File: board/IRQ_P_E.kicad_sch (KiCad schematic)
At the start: 18 parts, among them IC5 74LS189, IC6 74LS189, IC7 74LS189, IC8 74LS189, U42 74157, U43 74157, U44 74148, U45 74148, U46 74F32

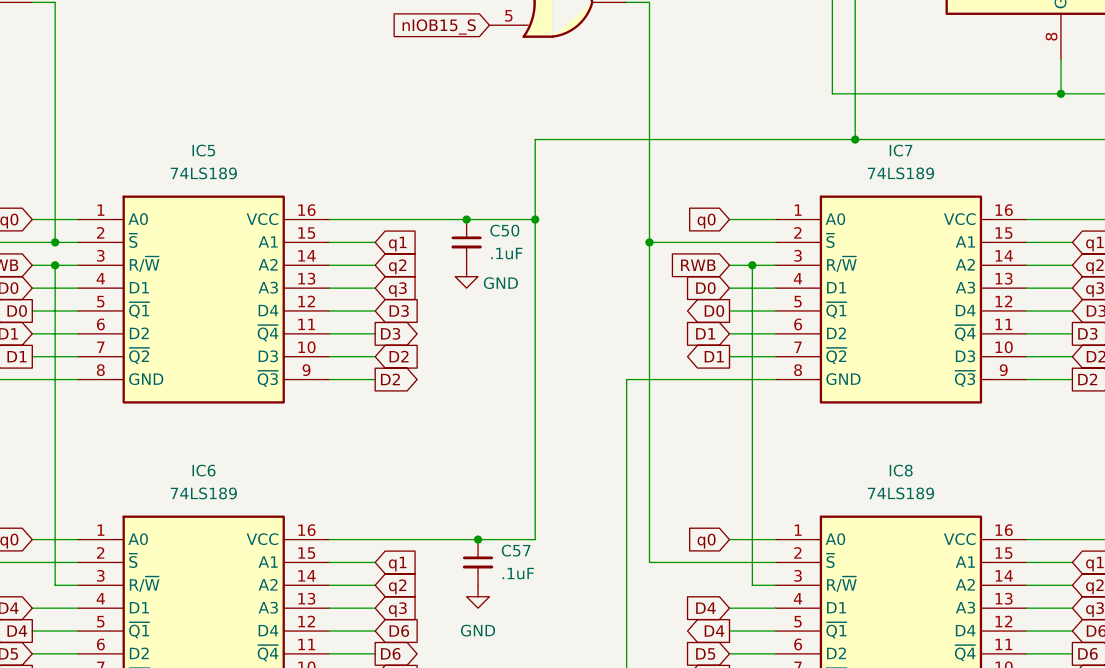
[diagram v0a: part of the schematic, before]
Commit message: Motherboard update with fill and traces.
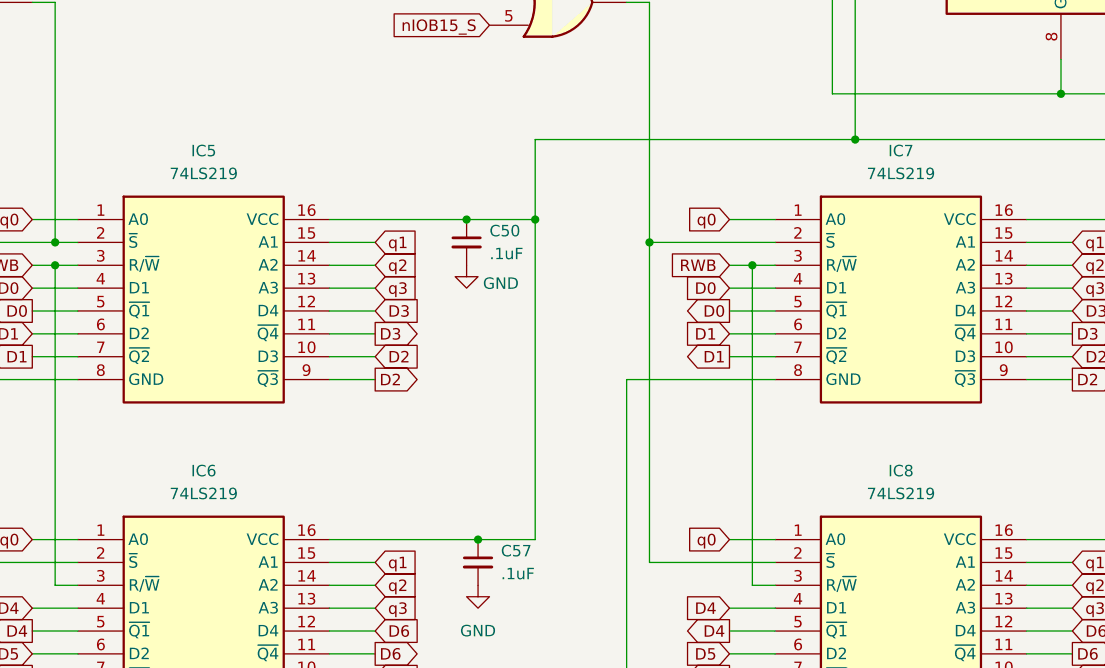
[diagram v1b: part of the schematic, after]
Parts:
- IC5, IC6, IC7, IC8: value 74LS189 -> 74LS219
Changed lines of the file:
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@@
 			)
 		)
-		(property "Value" "74LS189"
+		(property "Value" "74LS219"
 			(at 60.96 124.46 0)
 			(effects
@@
 			)
 		)
-		(property "Value" "74LS189"
+		(property "Value" "74LS219"
 			(at 60.96 160.02 0)
 			(effects
@@
 			)
 		)
-		(property "Value" "74LS189"
+		(property "Value" "74LS219"
 			(at 138.43 124.46 0)
 			(effects
@@
 			)
 		)
-		(property "Value" "74LS189"
+		(property "Value" "74LS219"
 			(at 138.43 160.02 0)
 			(effects

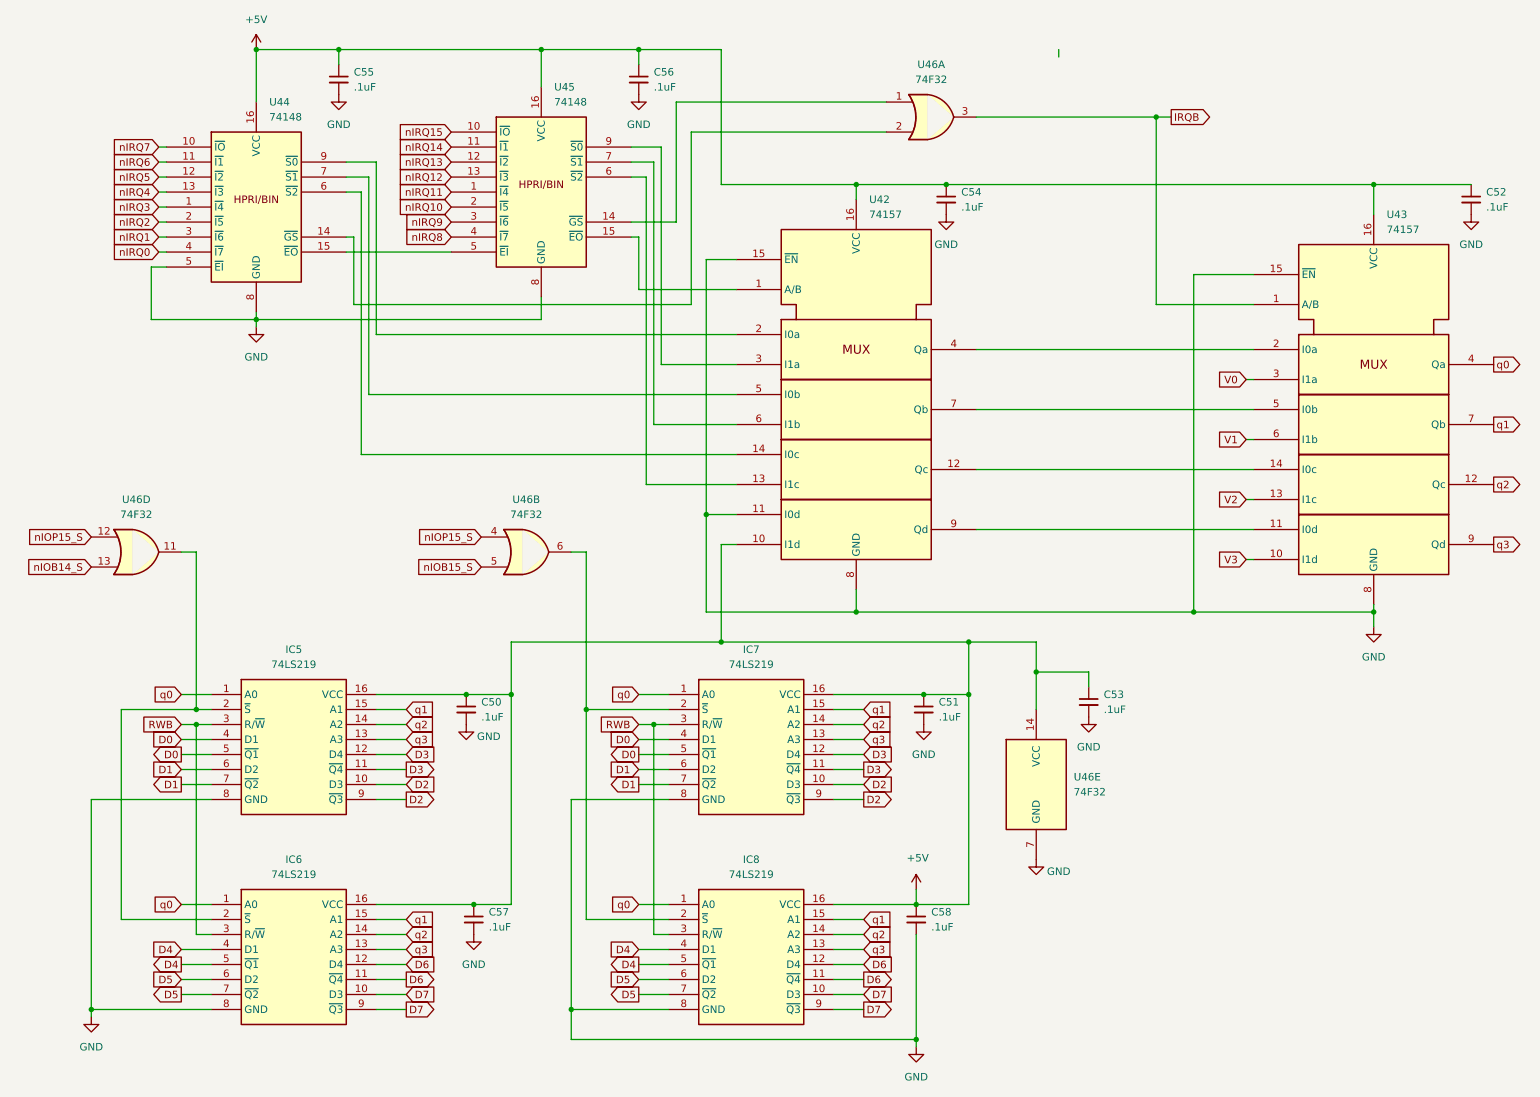
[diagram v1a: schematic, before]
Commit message: More main PCB updates.  Rearranged some things.  Bypass caps near PS connector.  Moved front panel connector to opposite side of board.
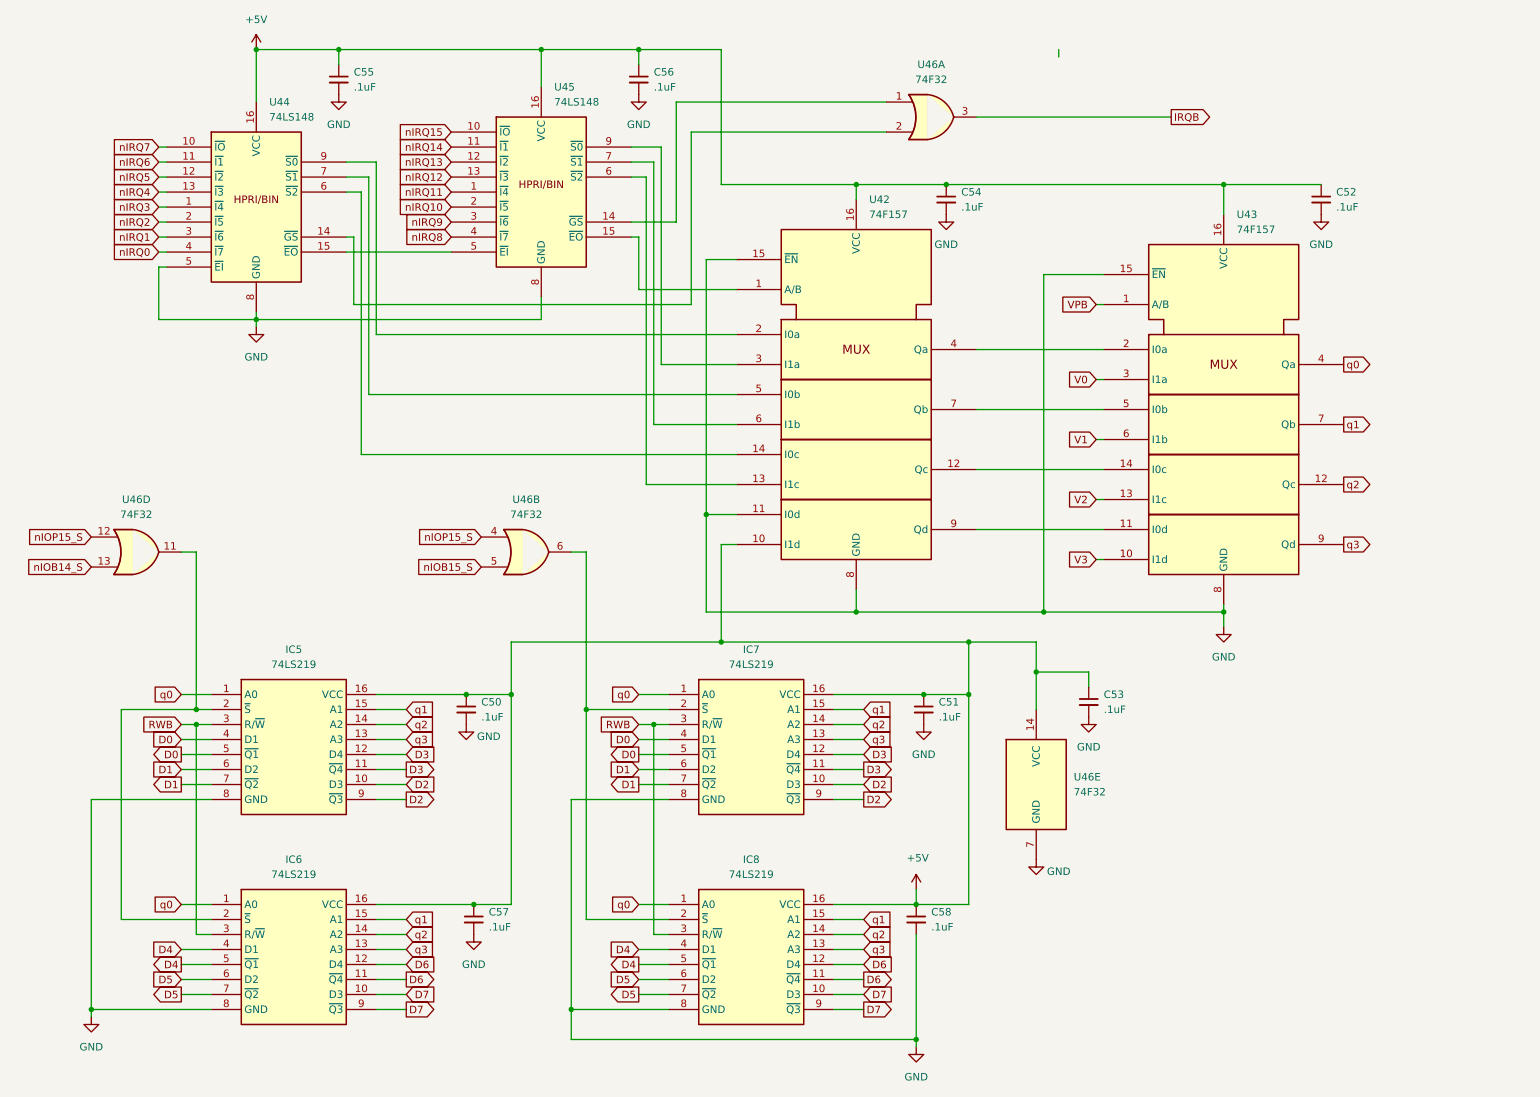
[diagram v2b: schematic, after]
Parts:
- IC5, IC6, IC7, IC8: footprint Package_DIP:DIP-16_W7.62mm_LongPads -> Package_DIP:DIP-16_W7.62mm_Socket_LongPads
- U42, U43: value 74157 -> 74F157
- U44, U45: value 74148 -> 74LS148
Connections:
- net IRQB: no longer U43.1 (A/B)
- new net VPB: U43.1 (A/B)
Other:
- moved on the sheet: C52, U43

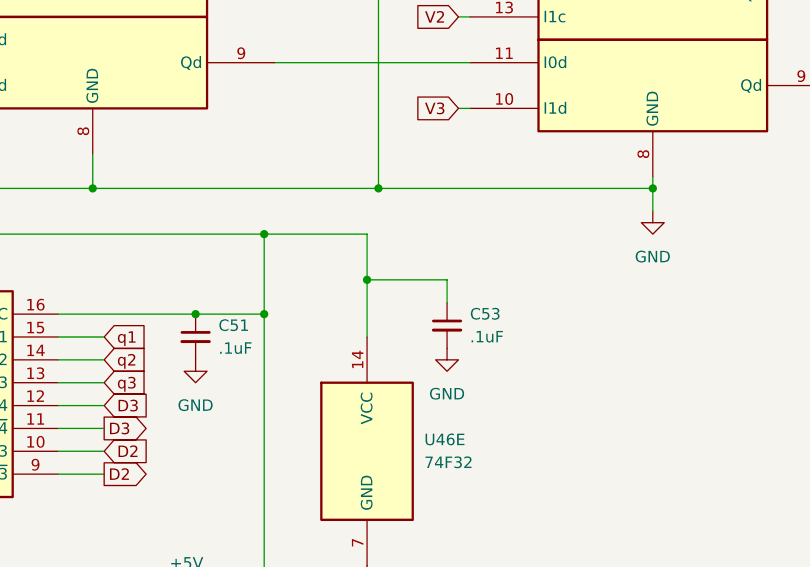
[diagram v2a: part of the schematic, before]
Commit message: Latest main PCB update with FFF1 and FFF2 added and decode logic updated to exclude FFFE and FFFF in nOSROM_S signal
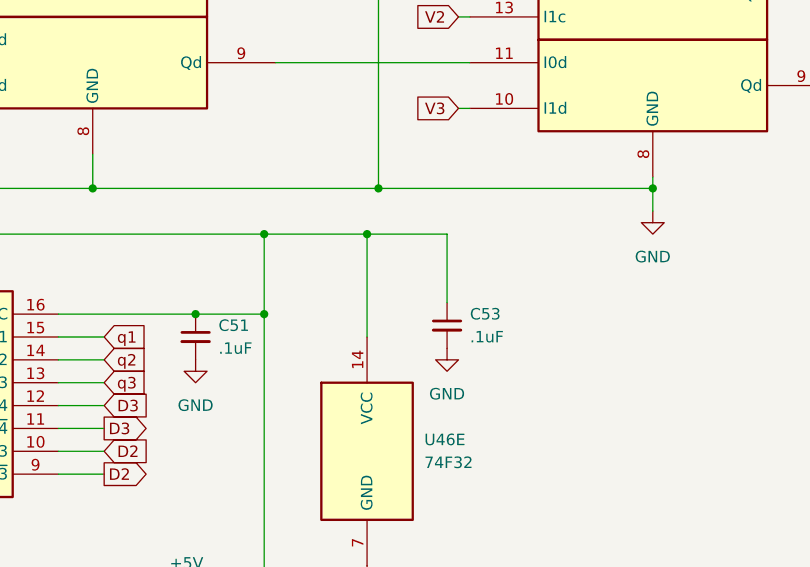
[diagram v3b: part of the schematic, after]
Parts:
- U42, U43, U44, U45: footprint Package_DIP:DIP-16_W7.62mm_LongPads -> Package_DIP:DIP-16_W7.62mm_Socket_LongPads
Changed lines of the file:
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@@
 	)
 	(junction
+		(at 186.69 120.65)
+		(diameter 0)
+		(color 0 0 0 0)
+	)
+	(junction
 		(at 130.81 99.06)
 		(diameter 0)
@@
 	)
 	(junction
-		(at 186.69 125.73)
-		(diameter 0)
-		(color 0 0 0 0)
-	)
-	(junction
 		(at 68.58 20.32)
 		(diameter 0)
@@
 	(wire
 		(pts
+			(xy 186.69 120.65) (xy 186.69 132.08)
+		)
+		(stroke
+			(width 0)
+			(type default)
+		)
+	)
+	(wire
+		(pts
 			(xy 123.19 36.83) (xy 123.19 73.66)
 		)
@@
 	(wire
 		(pts
-			(xy 195.58 125.73) (xy 186.69 125.73)
+			(xy 195.58 120.65) (xy 186.69 120.65)
 		)
 		(stroke
@@
 	(wire
 		(pts
-			(xy 186.69 120.65) (xy 186.69 125.73)
-		)
-		(stroke
-			(width 0)
-			(type default)
-		)
-	)
-	(wire
-		(pts
 			(xy 91.44 165.1) (xy 97.79 165.1)
 		)
@@
 	(wire
 		(pts
-			(xy 186.69 125.73) (xy 186.69 132.08)
-		)
-		(stroke
-			(width 0)
-			(type default)
-		)
-	)
-	(wire
-		(pts
 			(xy 152.4 177.8) (xy 157.48 177.8)
 		)
@@
 	(wire
 		(pts
-			(xy 195.58 128.27) (xy 195.58 125.73)
+			(xy 195.58 128.27) (xy 195.58 120.65)
 		)
 		(stroke
@@
 			)
 		)
-		(property "Footprint" "Package_DIP:DIP-16_W7.62mm_LongPads"
+		(property "Footprint" "Package_DIP:DIP-16_W7.62mm_Socket_LongPads"
 			(at 156.21 76.2 0)
 			(effects
@@
 			)
 		)
-		(property "Footprint" "Package_DIP:DIP-16_W7.62mm_LongPads"
+		(property "Footprint" "Package_DIP:DIP-16_W7.62mm_Socket_LongPads"
 			(at 102.87 44.45 0)
 			(effects
@@
 			)
 		)
-		(property "Footprint" "Package_DIP:DIP-16_W7.62mm_LongPads"
+		(property "Footprint" "Package_DIP:DIP-16_W7.62mm_Socket_LongPads"
 			(at 54.61 46.99 0)
 			(effects
@@
 			)
 		)
-		(property "Footprint" "Package_DIP:DIP-16_W7.62mm_LongPads"
+		(property "Footprint" "Package_DIP:DIP-16_W7.62mm_Socket_LongPads"
 			(at 218.44 78.74 0)
 			(effects

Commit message: Updated schematics with larger mounting holes (4mm vs 3.2mm) and larger electrolytic cap footprints
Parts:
- U46: footprint Package_DIP:DIP-14_W7.62mm_LongPads -> Package_DIP:DIP-14_W7.62mm_Socket_LongPads
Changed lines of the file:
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@@
 			)
 		)
-		(property "Footprint" "Package_DIP:DIP-14_W7.62mm_LongPads"
+		(property "Footprint" "Package_DIP:DIP-14_W7.62mm_Socket_LongPads"
 			(at 186.69 144.78 0)
 			(effects
@@
 			)
 		)
-		(property "Footprint" "Package_DIP:DIP-14_W7.62mm_LongPads"
+		(property "Footprint" "Package_DIP:DIP-14_W7.62mm_Socket_LongPads"
 			(at 34.29 105.41 0)
 			(effects
@@
 			)
 		)
-		(property "Footprint" "Package_DIP:DIP-14_W7.62mm_LongPads"
+		(property "Footprint" "Package_DIP:DIP-14_W7.62mm_Socket_LongPads"
 			(at 168.91 31.75 0)
 			(effects
@@
 			)
 		)
-		(property "Footprint" "Package_DIP:DIP-14_W7.62mm_LongPads"
+		(property "Footprint" "Package_DIP:DIP-14_W7.62mm_Socket_LongPads"
 			(at 100.33 105.41 0)
 			(effects
